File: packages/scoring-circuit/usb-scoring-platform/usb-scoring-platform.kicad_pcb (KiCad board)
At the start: 4 copper layers, 160 x 100 mm, 153 parts, among them J1 GCT USB4105-GF-A, J10 5520250-2, J2 STM SWD 3.3V, J3 LEFT WEAPON A B C, J4 RIGHT WEAPON A B C, J5 PISTE - NOT protective earth, J6 ESP 3.3V UART recovery, J7 TST-108-02-G-D - HUB75, J8 645004114822 - panel 5V, J9 5520250-2, Q1 BSS138-7-F, Q2 BSS138-7-F, Q3 BSS138-7-F, SW1 STM RESET, SW2 ESP RESET, SW3 ESP BOOT, U1 STM32G474RET6, U10 SN74AXC1T45DCKR, U11 SN74AXC1T45DCKR, U12 WIZ850io, U13 TSOP38438, U14 SN74AHCT245PWR, U15 SN74AHCT245PWR, U16 4N32M, U17 4N32M, U18 LTM2884IY#PBF, U2 ESP32-S3-WROOM-1-N8R8, U3 USBLC6-2SC6, U4 AP2112K-3.3TRG1, U5 Adafruit 5807 - set 20V, U6 D36V50F5, U7 AP63203WU-7, U8 74LVC125APW, U9 74LVC125APW, Y1 ABM3B-8.000MHZ-B2-T

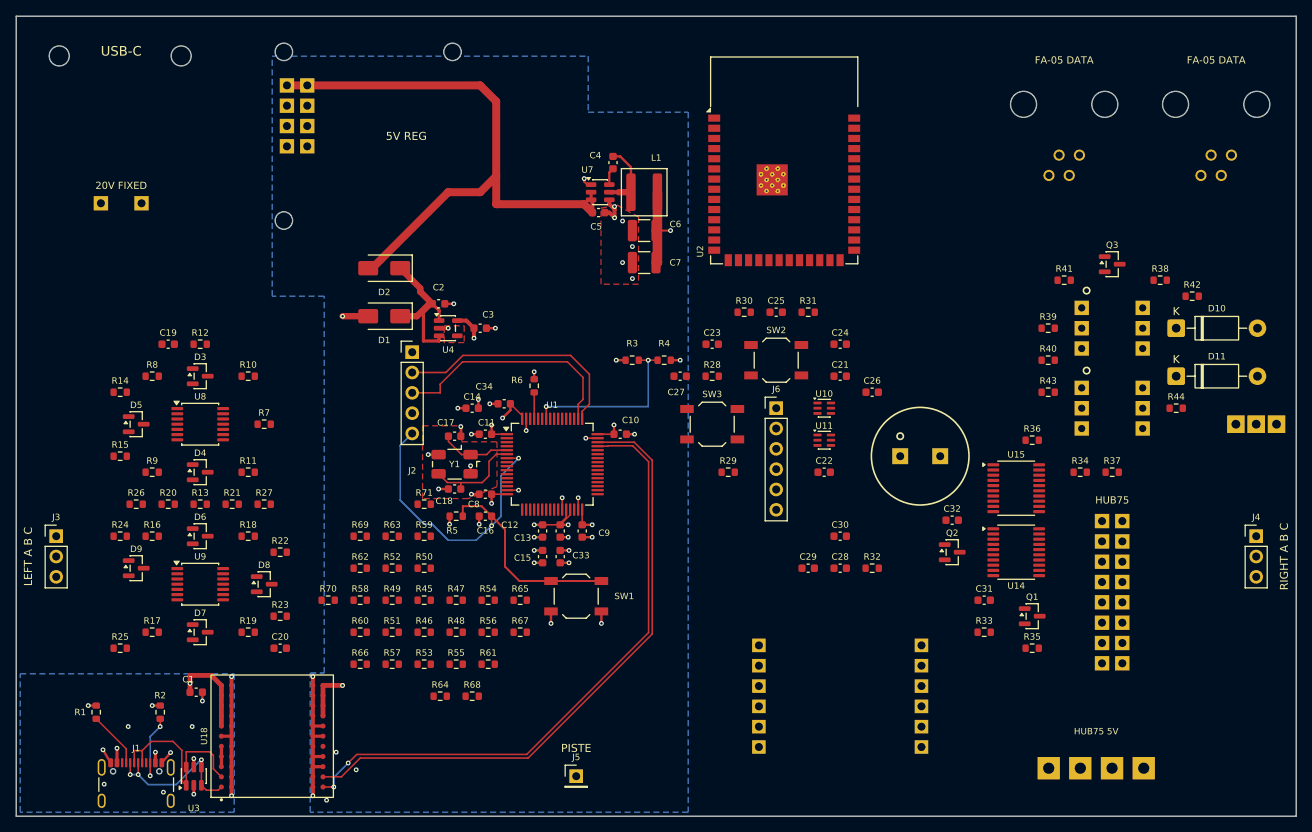
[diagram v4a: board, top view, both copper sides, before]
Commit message: feat(scoring-circuit): route PD and display power distribution
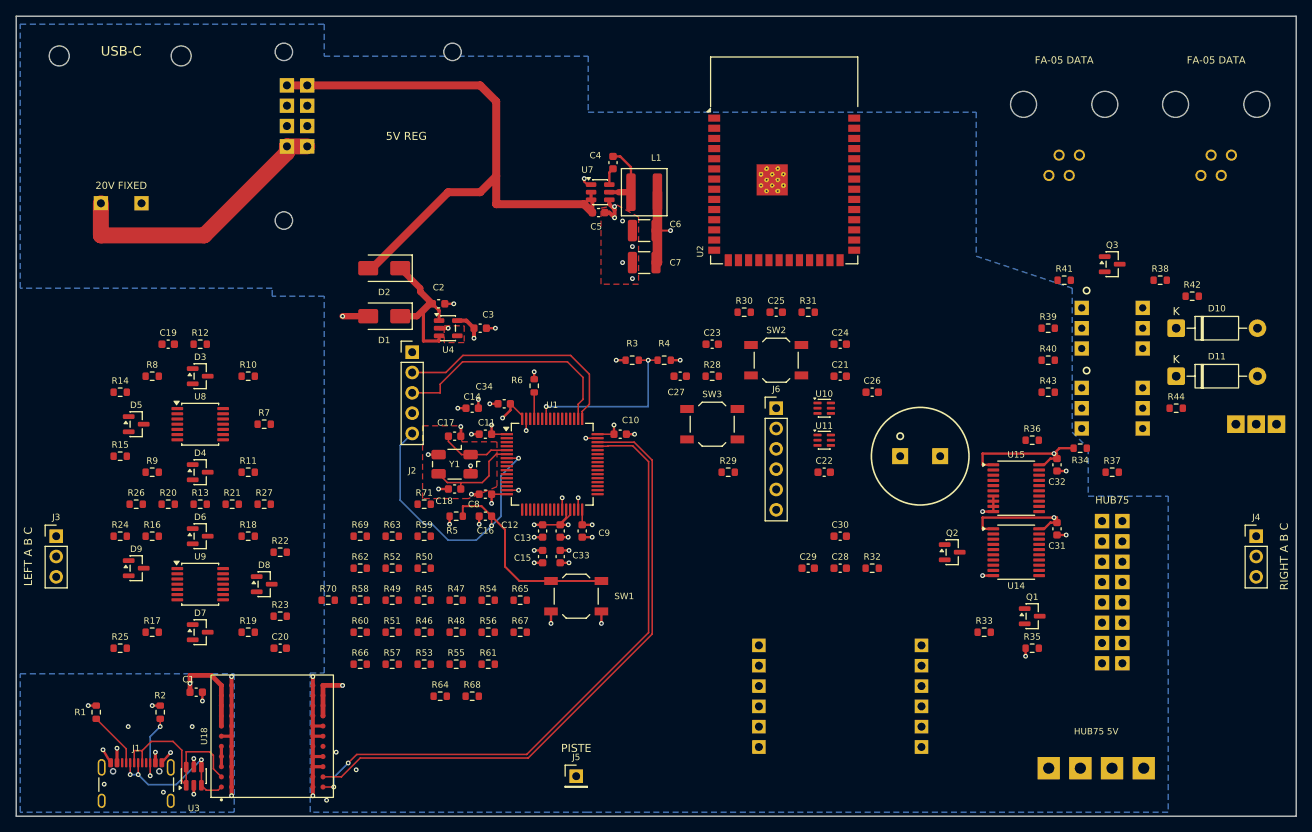
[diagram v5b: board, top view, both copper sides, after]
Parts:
- moved C32 14.8 mm to (180.1, 106.1), turned to -90 degrees
- moved C31 12.7 mm to (180.1, 114.1), turned to -90 degrees
- moved R34 3.00 mm to (183.0, 104.0)
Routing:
- net PD_20V: track 0.00 -> 34.9 mm
- net PANEL_5V: track 75.7 -> 109.9 mm, vias 0 -> 3
- net GND: track 56.1 -> 63.1 mm, vias 38 -> 42
- added copper zone on In2.Cu, net PANEL_5V

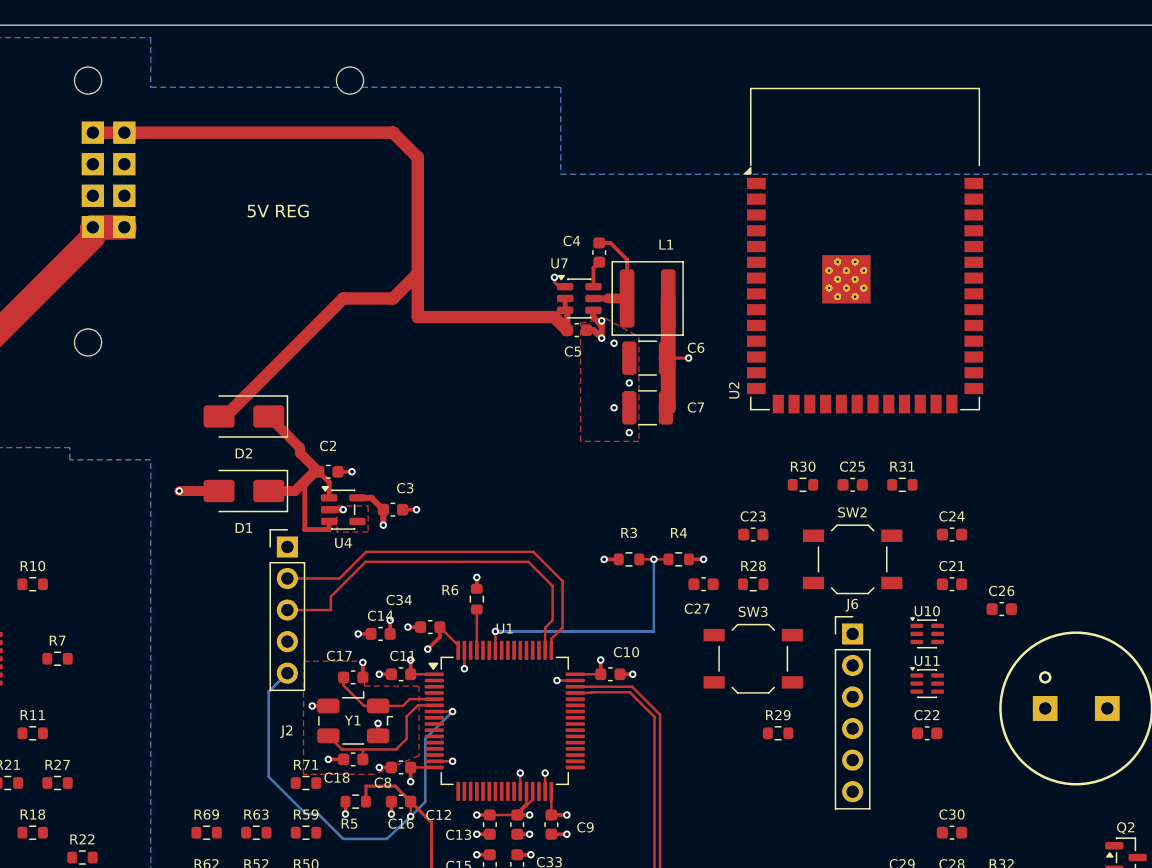
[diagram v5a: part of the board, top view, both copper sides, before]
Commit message: feat(scoring-circuit): route ESP32 power and recovery support
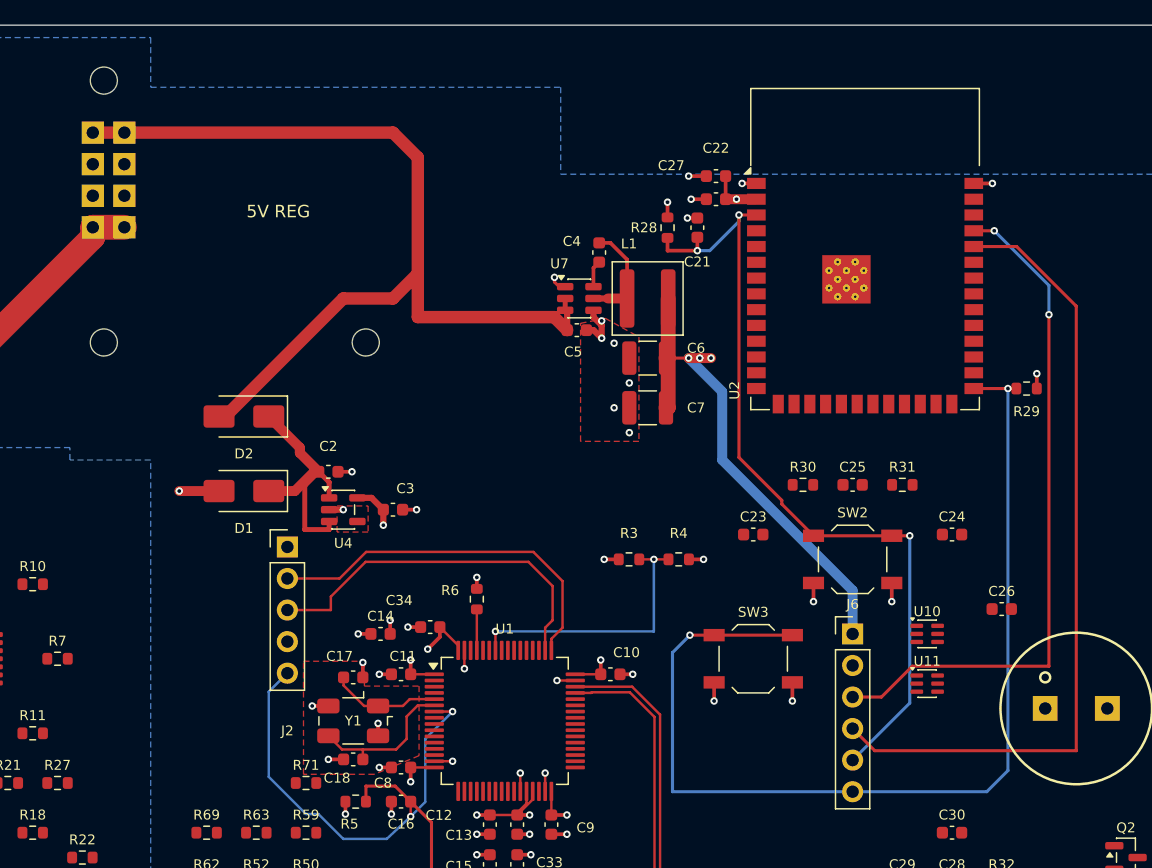
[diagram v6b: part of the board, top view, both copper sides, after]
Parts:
- moved C22 46.2 mm to (134.0, 64.0), turned to 180 degrees
- moved C21 35.3 mm to (132.5, 66.3), turned to 90 degrees
- moved R29 34.2 mm to (159.0, 79.2), turned to 180 degrees
- moved C27 32.9 mm to (134.0, 62.1), turned to 180 degrees
- moved R28 29.5 mm to (130.1, 66.3), turned to -90 degrees
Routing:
- net ESP_BOOT0: track 0.00 -> 83.3 mm, vias 0 -> 2
- net ESP_EN: track 0.00 -> 66.8 mm, vias 0 -> 3
- net ESP_PROGRAM_RX: track 0.00 -> 64.8 mm
- net ESP_PROGRAM_TX: track 0.00 -> 55.3 mm, vias 0 -> 2
- net APP_3V3: track 27.3 -> 63.6 mm, vias 2 -> 7
- net GND: track 63.1 -> 75.2 mm, vias 42 -> 51
- added copper zone on In2.Cu, net APP_3V3

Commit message: feat(scoring-circuit): add black mask and Fencing Club silkscreen
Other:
- board text added: "Fencing Club"
